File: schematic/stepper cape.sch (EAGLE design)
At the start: 48 parts, among them J1 ISP, U1 CAT24C, U2 LM7805, X1 A4988BREAKOUT

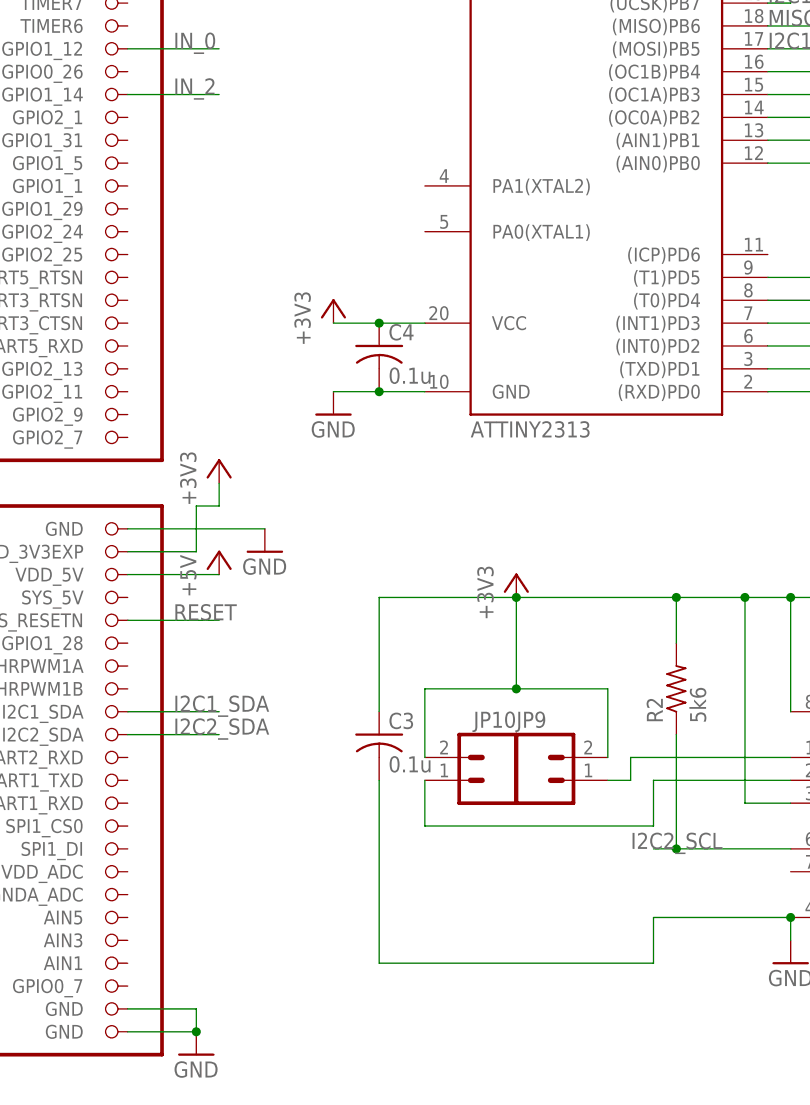
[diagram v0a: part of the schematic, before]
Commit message: Connected spare IO pins on AVR to inputs 0 and 1; changed to 0805 parts instead of 1206.
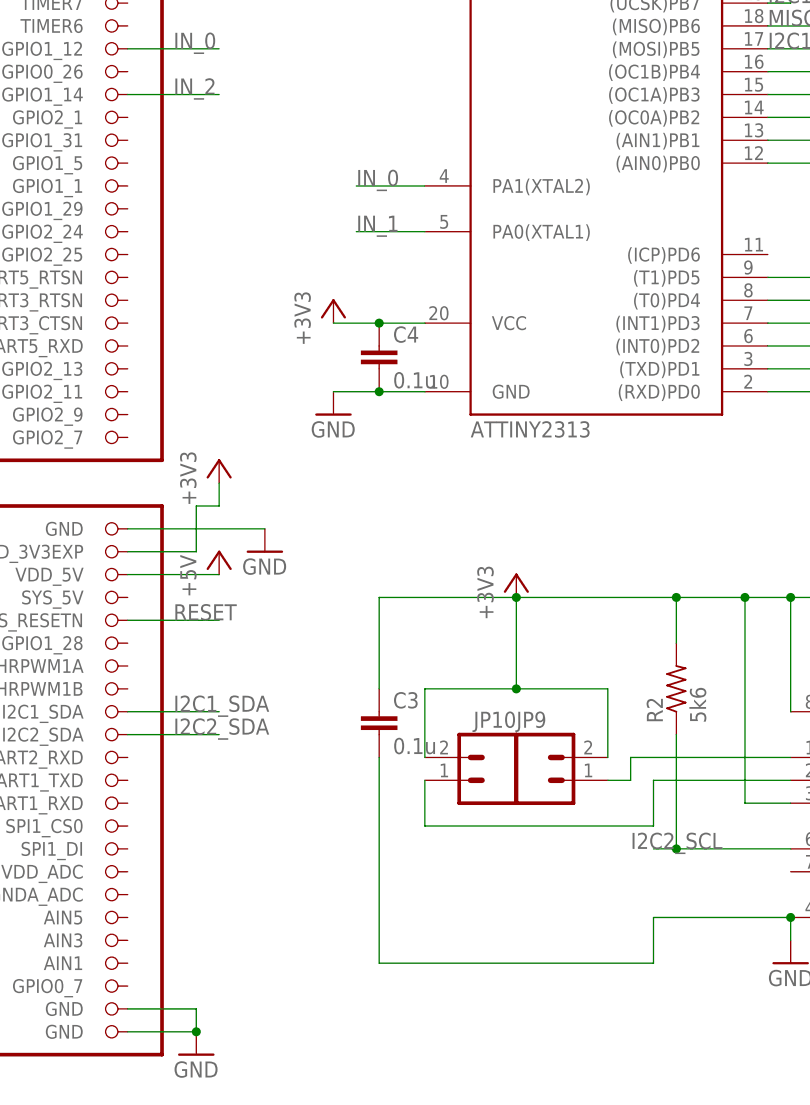
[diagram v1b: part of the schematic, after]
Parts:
- C3, C4: device adafruit:C-USC1206 -> SparkFun-Passives:CAP0805
- R1, R10, R11, R12, R13, R14, R15, R16, R17, R18, R2, R3, R4, R5, R6, R7, R8, R9: device adafruit:R-US_R1206 -> adafruit:R-US_R0805
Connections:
- net IN_0: now also U$2.PA1(XTAL2)
- net IN_1: now also U$2.PA0(XTAL1)
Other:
- moved on the sheet: C3
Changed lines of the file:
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@@
 <part name="+3V2" library="supply1" deviceset="+3V3" device=""/>
 <part name="+3V3" library="supply1" deviceset="+3V3" device=""/>
-<part name="R2" library="adafruit" deviceset="R-US_" device="R1206" value="5k6"/>
-<part name="R3" library="adafruit" deviceset="R-US_" device="R1206" value="5k6"/>
+<part name="R2" library="adafruit" deviceset="R-US_" device="R0805" value="5k6"/>
+<part name="R3" library="adafruit" deviceset="R-US_" device="R0805" value="5k6"/>
 <part name="GND9" library="supply1" deviceset="GND" device=""/>
-<part name="C3" library="adafruit" deviceset="C-US" device="C1206" value="0.1u"/>
+<part name="C3" library="SparkFun-Passives" deviceset="CAP" device="0805" value="0.1u"/>
 <part name="X" library="RepRapjr" deviceset="A4988BREAKOUT" device=""/>
 <part name="+3V5" library="supply1" deviceset="+3V3" device=""/>
@@
 <part name="LED3" library="adafruit" deviceset="LED" device="CHIPLED_1206"/>
 <part name="LED4" library="adafruit" deviceset="LED" device="CHIPLED_1206"/>
-<part name="R7" library="adafruit" deviceset="R-US_" device="R1206" value="1k"/>
-<part name="R8" library="adafruit" deviceset="R-US_" device="R1206" value="1k"/>
+<part name="R7" library="adafruit" deviceset="R-US_" device="R0805" value="1k"/>
+<part name="R8" library="adafruit" deviceset="R-US_" device="R0805" value="1k"/>
 <part name="+3V6" library="supply1" deviceset="+3V3" device=""/>
 <part name="X1" library="RepRapjr" deviceset="A4988BREAKOUT" device=""/>
@@
 <part name="LED7" library="adafruit" deviceset="LED" device="CHIPLED_1206"/>
 <part name="LED8" library="adafruit" deviceset="LED" device="CHIPLED_1206"/>
-<part name="R4" library="adafruit" deviceset="R-US_" device="R1206" value="1k"/>
-<part name="R5" library="adafruit" deviceset="R-US_" device="R1206" value="1k"/>
-<part name="R6" library="adafruit" deviceset="R-US_" device="R1206" value="4k7"/>
-<part name="R9" library="adafruit" deviceset="R-US_" device="R1206" value="4k7"/>
+<part name="R4" library="adafruit" deviceset="R-US_" device="R0805" value="1k"/>
+<part name="R5" library="adafruit" deviceset="R-US_" device="R0805" value="1k"/>
+<part name="R6" library="adafruit" deviceset="R-US_" device="R0805" value="4k7"/>
+<part name="R9" library="adafruit" deviceset="R-US_" device="R0805" value="4k7"/>
 <part name="JP5" library="SparkFun-Connectors" deviceset="M03" device="PTH"/>
 <part name="P+7" library="supply1" deviceset="+5V" device=""/>
-<part name="R10" library="adafruit" deviceset="R-US_" device="R1206" value="10k"/>
-<part name="R11" library="adafruit" deviceset="R-US_" device="R1206" value="20k"/>
+<part name="R10" library="adafruit" deviceset="R-US_" device="R0805" value="10k"/>
+<part name="R11" library="adafruit" deviceset="R-US_" device="R0805" value="20k"/>
 <part name="GND14" library="supply1" deviceset="GND" device=""/>
 <part name="JP6" library="SparkFun-Connectors" deviceset="M03" device="PTH"/>
 <part name="P+8" library="supply1" deviceset="+5V" device=""/>
-<part name="R12" library="adafruit" deviceset="R-US_" device="R1206" value="10k"/>
-<part name="R13" library="adafruit" deviceset="R-US_" device="R1206" value="20k"/>
+<part name="R12" library="adafruit" deviceset="R-US_" device="R0805" value="10k"/>
+<part name="R13" library="adafruit" deviceset="R-US_" device="R0805" value="20k"/>
 <part name="GND15" library="supply1" deviceset="GND" device=""/>
 <part name="JP7" library="SparkFun-Connectors" deviceset="M03" device="PTH"/>
 <part name="P+9" library="supply1" deviceset="+5V" device=""/>
-<part name="R14" library="adafruit" deviceset="R-US_" device="R1206" value="10k"/>
-<part name="R15" library="adafruit" deviceset="R-US_" device="R1206" value="20k"/>
+<part name="R14" library="adafruit" deviceset="R-US_" device="R0805" value="10k"/>
+<part name="R15" library="adafruit" deviceset="R-US_" device="R0805" value="20k"/>
 <part name="GND16" library="supply1" deviceset="GND" device=""/>
 <part name="JP8" library="SparkFun-Connectors" deviceset="M03" device="PTH"/>
 <part name="P+10" library="supply1" deviceset="+5V" device=""/>
-<part name="R16" library="adafruit" deviceset="R-US_" device="R1206" value="10k"/>
-<part name="R17" library="adafruit" deviceset="R-US_" device="R1206" value="20k"/>
+<part name="R16" library="adafruit" deviceset="R-US_" device="R0805" value="10k"/>
+<part name="R17" library="adafruit" deviceset="R-US_" device="R0805" value="20k"/>
 <part name="GND17" library="supply1" deviceset="GND" device=""/>
 <part name="U2" library="SparkFun-PowerIC" deviceset="V_REG_78XX" device="SINK" value="LM7805"/>
@@
 <part name="JP9" library="SparkFun-Connectors" deviceset="M02" device="PTH"/>
 <part name="JP10" library="SparkFun-Connectors" deviceset="M02" device="PTH"/>
-<part name="R1" library="adafruit" deviceset="R-US_" device="R1206" value="5k6"/>
-<part name="R18" library="adafruit" deviceset="R-US_" device="R1206" value="5k6"/>
-<part name="C4" library="adafruit" deviceset="C-US" device="C1206" value="0.1u"/>
+<part name="R1" library="adafruit" deviceset="R-US_" device="R0805" value="5k6"/>
+<part name="R18" library="adafruit" deviceset="R-US_" device="R0805" value="5k6"/>
+<part name="C4" library="SparkFun-Passives" deviceset="CAP" device="0805" value="0.1u"/>
 <part name="J1" library="SparkFun-Connectors" deviceset="AVR_SPI_PRG_6" device="PTH" value="ISP"/>
 <part name="+3V4" library="supply1" deviceset="+3V3" device=""/>
@@
 <instance part="R1" gate="G$1" x="147.32" y="134.62" rot="R90"/>
 <instance part="R18" gate="G$1" x="142.24" y="134.62" rot="R90"/>
-<instance part="C4" gate="G$1" x="96.52" y="88.9"/>
+<instance part="C4" gate="G$1" x="96.52" y="86.36"/>
 <instance part="J1" gate="G$1" x="299.72" y="91.44"/>
 <instance part="+3V4" gate="G$1" x="312.42" y="99.06"/>
@@
 <wire x1="142.24" y1="25.4" x2="142.24" y2="22.86" width="0.1524" layer="91"/>
 <pinref part="C3" gate="G$1" pin="2"/>
-<wire x1="96.52" y1="40.64" x2="96.52" y2="20.32" width="0.1524" layer="91"/>
+<wire x1="96.52" y1="43.18" x2="96.52" y2="20.32" width="0.1524" layer="91"/>
 <wire x1="96.52" y1="20.32" x2="127" y2="20.32" width="0.1524" layer="91"/>
 <wire x1="127" y1="20.32" x2="127" y2="25.4" width="0.1524" layer="91"/>
@@
 <pinref part="C3" gate="G$1" pin="1"/>
 <wire x1="111.76" y1="60.96" x2="96.52" y2="60.96" width="0.1524" layer="91"/>
-<wire x1="96.52" y1="60.96" x2="96.52" y2="48.26" width="0.1524" layer="91"/>
+<wire x1="96.52" y1="60.96" x2="96.52" y2="50.8" width="0.1524" layer="91"/>
 <pinref part="U1" gate="A" pin="A2"/>
 <wire x1="137.16" y1="38.1" x2="142.24" y2="38.1" width="0.1524" layer="91"/>
@@
 <label x="292.1" y="58.42" size="1.778" layer="95"/>
 </segment>
+<segment>
+<pinref part="U$2" gate="G$1" pin="PA1(XTAL2)"/>
+<wire x1="101.6" y1="106.68" x2="93.98" y2="106.68" width="0.1524" layer="91"/>
+<label x="93.98" y="106.68" size="1.778" layer="95"/>
+</segment>
 </net>
 <net name="IN_1" class="0">
@@
 <label x="259.08" y="58.42" size="1.778" layer="95"/>
 </segment>
-</net>
+<segment>
+<pinref part="U$2" gate="G$1" pin="PA0(XTAL1)"/>
+<wire x1="101.6" y1="101.6" x2="93.98" y2="101.6" width="0.1524" layer="91"/>
+<label x="93.98" y="101.6" size="1.778" layer="95"/>
+</segment>
+</net>
